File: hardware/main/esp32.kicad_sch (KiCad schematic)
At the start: 15 parts, among them U1 ESP32-S3-WROOM-1

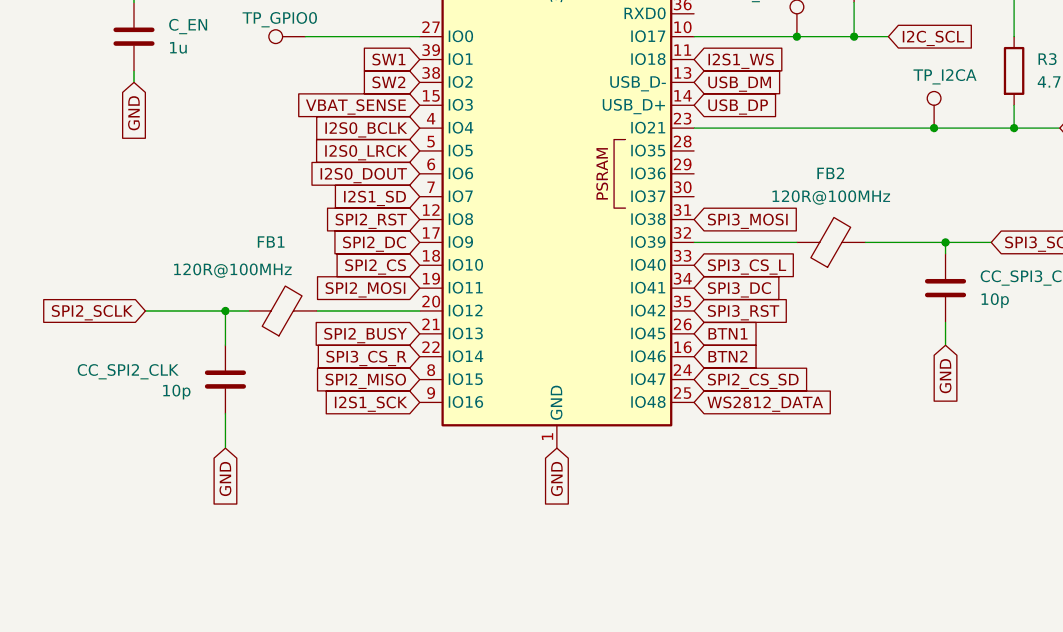
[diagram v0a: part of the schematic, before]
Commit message: hardware: pull-ups carte SD, resistances serie d'horloge, timer de charge
Trois points "important" de l'audit 2026-09-23, verifies un par un sur le
schema avant modification (tools/kicad_netlist.py).

H7 — carte SD : aucune pull-up sur J11. L'ESP-IDF les rend obligatoires
(sd_pullup_requirements.rst : « en mode SPI ou SD 1 bit, CMD et DAT0-DAT3
doivent etre tirees au plus par 10k, y compris les lignes non reliees a
l'hote »). Ajout de R15-R19 (10k) sur un rail 3V3_D commun, feuille connector.
DAT1 (J11.8) et DAT2 (J11.1) n'avaient aucun fil : nets nommes SD_DAT1/SD_DAT2.

H8 — horloges SPI : FB1/FB2 (ferrites 120R) remplacees par R13/R14 = 22 ohm
0603. Device:R et Device:FerriteBead ont leurs pins au meme endroit, donc les
fils et la connectivite sont inchanges. Une ferrite sur une horloge rapide
arrondit les fronts et viole les timings de la carte (ESP-IDF sdspi_share.rst,
AC loading) ; les yeux tournent a 40 MHz, 80 visees. Ajout de C6/C7, 10 pF vers
GND en DNP, comme provision jusqu'au test CEM.

H9 — charge LiPo : TMR etait cable directement a GND, c'est-a-dire timers de
securite desactives (bq24075 §6.1). Ajout de R_TMR 56k 1 % entre TMR et GND
-> t_MAXCHG = 10 x K_TMR x R_TMR = 5,6 a 9,3 h (K_TMR 36-60 s/kOhm), pour une
charge de ~4 h a 1 A sur 3000 mAh. Plage admissible datasheet : 18-72 kOhm.

A4 — ICS-43434 sans decouplage : CONSTAT ERRONE, aucune modification faite.
C3 (100 nF 0402, 3V3_A/GND) est deja place a cote de U4 et l'etait deja dans le
fichier du 23/09. Seule subsiste une contrainte de layout (au plus pres des
broches 5 et 3, sans via). Le rapport d'audit et la fiche datasheet sont annotes
en consequence.

tools/kicad_edit.py : helpers d'edition de schema (symboles, fils, labels,
jonctions, remplacement de composant a geometrie de pins identique).
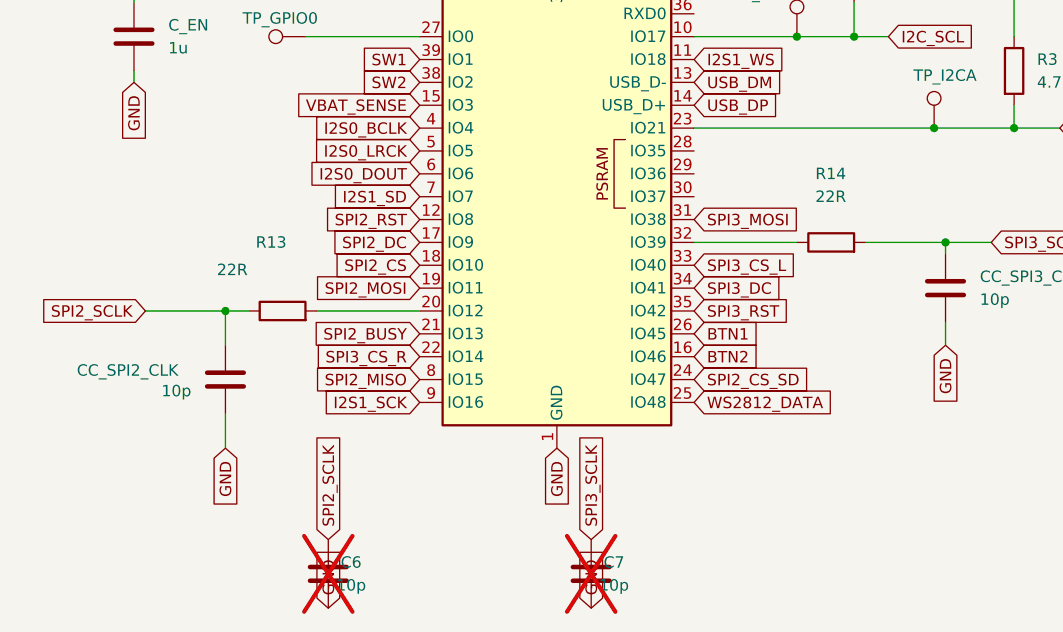
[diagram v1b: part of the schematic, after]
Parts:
- added C6, C7: 10p, Capacitor_SMD:C_0402_1005Metric, symbol Device:C
- R13: renamed from FB1; value 120R@100MHz -> 22R; footprint Inductor_SMD:L_0603_1608Metric -> Resistor_SMD:R_0603_1608Metric; symbol Device:FerriteBead -> Device:R
- R14: renamed from FB2; value 120R@100MHz -> 22R; footprint Inductor_SMD:L_0603_1608Metric -> Resistor_SMD:R_0603_1608Metric; symbol Device:FerriteBead -> Device:R
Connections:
- net GND: now also C6.2, C7.2
- net SPI2_SCLK: now also C6.1
- net SPI3_SCLK: now also C7.1

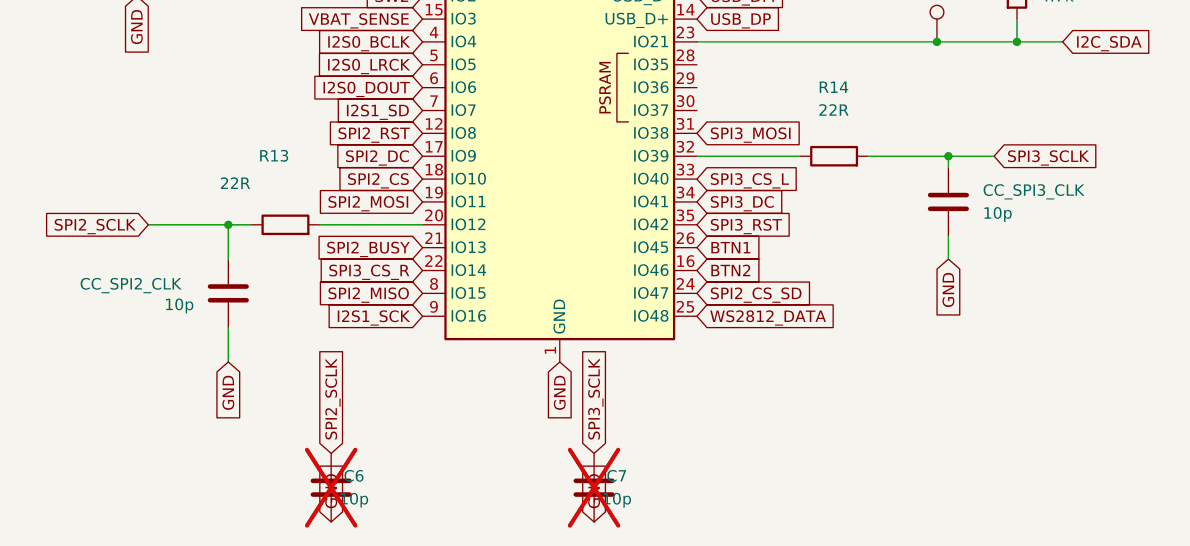
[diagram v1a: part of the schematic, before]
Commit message: hardware(power): U5 (3V3_D) en SO-8 — AP2112M-3.3TRG1
Audit 2026-09-23 H5 : en SOT-25 (theta JA 184 C/W), U5 dissipe 0,56 W sous USB
a 400 mA, soit +103 C d'elevation en boitier ferme. Le SO-8 (114 C/W) ramene
l'elevation a +64 C — meilleur que le SOT-89-5 envisage dans l'audit (120 C/W),
et surtout disponible chez LCSC (C5290219), ce que n'etait pas le SOT-89-5.

U6 (3V3_A) reste en SOT-25 : il n'alimente que le PCM5122, ~25 mA, il ne
chauffe pas. Deux references du meme LDO dans la BOM, assume.

Brochage SO-8 releve sur le dessin de la datasheet (le tableau correspondant
n'est pas extractible en texte, et les sources web se contredisaient) :
1 = VOUT, 2/3/4 = NC, 5 = EN, 6+7 = GND, 8 = VIN. Il n'a rien de commun avec
celui du SOT-25 (1 = VIN, 2 = GND, 3 = EN, 5 = VOUT).

Symbole : la bibliotheque KiCad officielle ne contient que les variantes K
(SOT-25), le symbole a donc ete cree dans la bibliotheque projet
`lcsc_imported`, avec les positions de broches du symbole officiel — VIN, EN et
VOUT retombent ainsi exactement sur les fils deja en place. Seules les deux
masses (6 et 7) ont demande un fil, et le global label GND existant se trouvait
deja pile entre elles.

Verifie par netlist : VIN->VSYS, EN->EN_SYS, VOUT->3V3_D, GND sur les deux
broches, 3V3_D intact avec ses 28 consommateurs, U6 inchange.

Reste a faire au layout : plan de cuivre genereux sous et autour de U5.
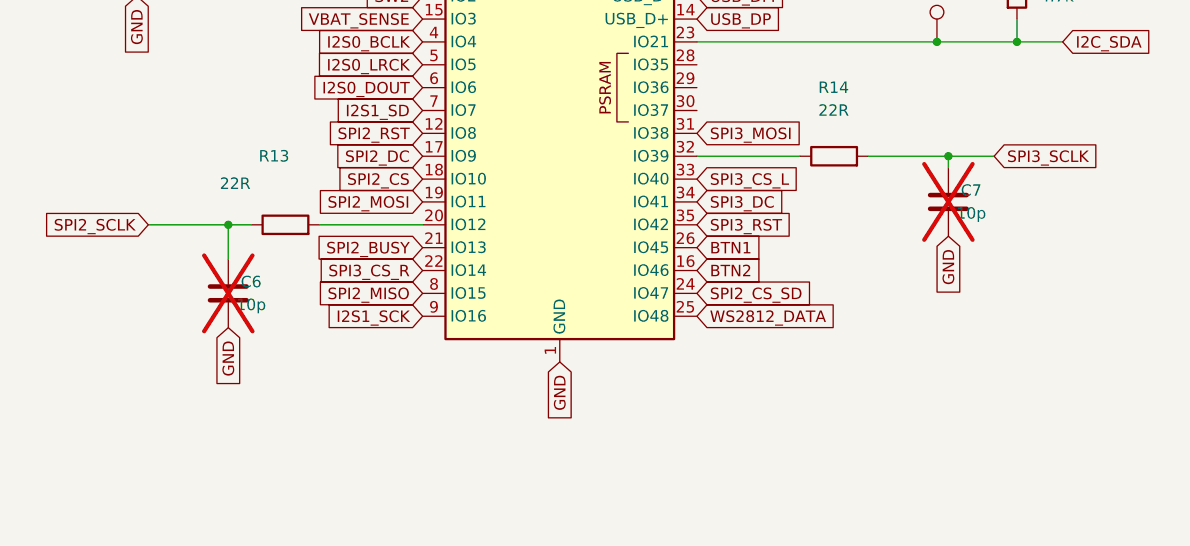
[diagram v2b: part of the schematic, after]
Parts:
- removed CC_SPI2_CLK, CC_SPI3_CLK: 10p, Capacitor_SMD:C_0402_1005Metric, symbol Device:C
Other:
- moved on the sheet: C6, C7

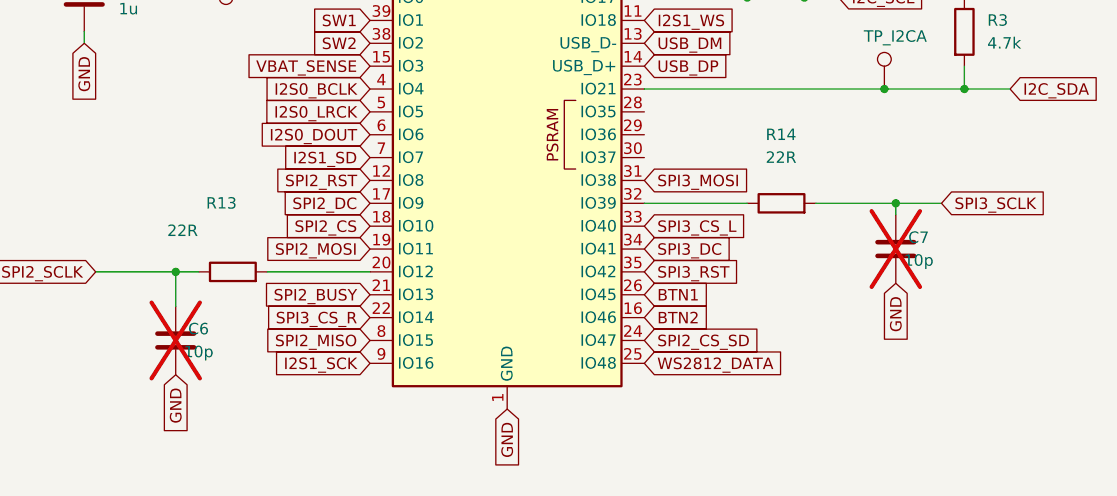
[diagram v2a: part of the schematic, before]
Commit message: hardware+tools: BOM reconciliee avec le schema + controleur automatique
Controle complet demande apres la decouverte que la BOM avait derive. Nouvel
outil tools/check_bom.py : verifie references manquantes des deux cotes,
quantites, valeurs et empreintes, et liste les champs LCSC absents. Il
normalise les notations (4u7 vs 4.7uF, 1k5 vs 1.5k) pour ne pas crier au loup.

Ecarts trouves et corrigés :
- 33 composants du schema ne figuraient PAS dans la BOM, tous preexistants :
  les 12 WS2812 du halo, les 7 condensateurs du PAM8406, C_U9, C_VBAT_SENSE,
  8 resistances nommees (R_MUTE, R_SHDN, R_MODE_*, R_SD_PD, R_CS, R_VBAT_*) et
  les 4 points de test. La carte n'aurait pas pu etre assemblee telle quelle.
- CONFLIT DE REFERENCE de ma part : mes deux 10 pF de provision CEM utilisaient
  C6 et C7, que la BOM reservait deja a des decouplages generiques. Renommes
  C_CLK2 et C_CLK3.
- C1 etait compte dans le groupe « 100nF 0402 » alors que le schema en fait un
  10 uF 0603 (reservoir au pied du module ESP32). Ligne propre.
- R7 (ex-RSTPD du PN532, parti sur un satellite) et C8-C12 : reliquats retires.
- R_MODE_AB documentee comme DNP avec l'avertissement correspondant : montee en
  meme temps que R_MODE_D, elle ferait un diviseur sur l'entree MODE du
  PAM8406. Le schema, lui, etait deja correct (dnp=yes).

Resultat du controle : 0 reference manquante, 0 quantite incoherente, 0
divergence de valeur ou d'empreinte. Reste la dette connue des 93 champs LCSC.

ERC : 148 -> 139 warnings, toujours 0 erreur. Le fil non connecte et les trois
empreintes JST introuvables ont disparu. Subsiste un lib_symbol_mismatch sur
Conn_01x03 : symbole pris dans la bibliotheque v9 (seule accessible) alors que
le projet est en KiCad 10 — a resoudre d'un « Update Symbol from Library »,
la bibliotheque locale faisant foi.
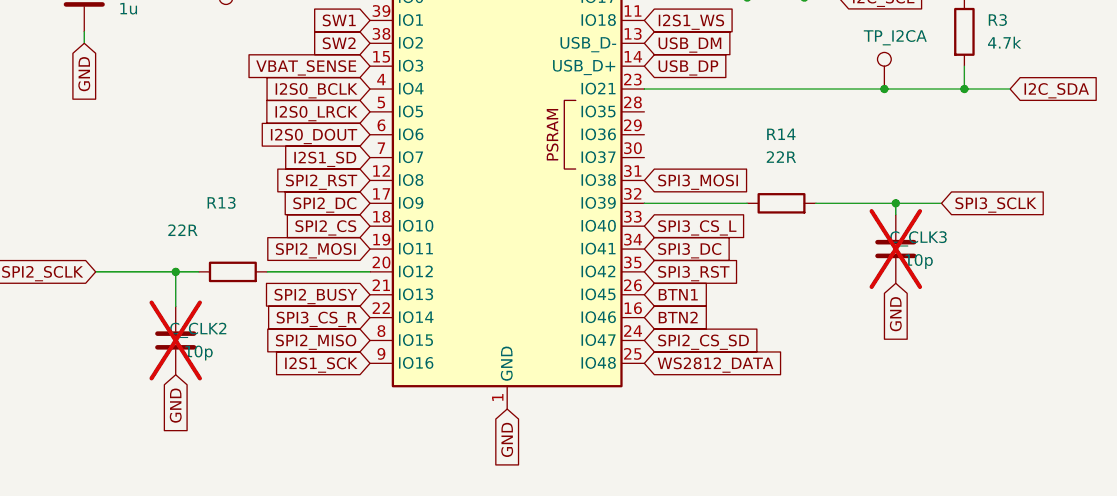
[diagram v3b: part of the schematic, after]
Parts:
- renumbered C6 to C_CLK2, C7 to C_CLK3
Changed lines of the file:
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@@
 		(in_pos_files yes)
 		(dnp yes)
-		(property "Reference" "C7"
+		(property "Reference" "C_CLK3"
 			(at 191.77 99.06 0)
 			(show_name no)
@@
 			(project "blackbox"
 				(path "/49e0257f-ff47-4890-a1ac-89438fa62044/14cfff57-6a31-4c05-af76-83111480b025"
-					(reference "C7")
+					(reference "C_CLK3")
 					(unit 1)
 				)
@@
 		(in_pos_files yes)
 		(dnp yes)
-		(property "Reference" "C6"
+		(property "Reference" "C_CLK2"
 			(at 111.76 109.22 0)
 			(show_name no)
@@
 			(project "blackbox"
 				(path "/49e0257f-ff47-4890-a1ac-89438fa62044/14cfff57-6a31-4c05-af76-83111480b025"
-					(reference "C6")
-					(unit 1)
-				)
+					(reference "C_CLK2")
+					(unit 1)
+				)
